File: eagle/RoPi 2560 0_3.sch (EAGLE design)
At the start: 49 parts, among them J1 AVR_SPI_PRG_6PTH, U1 ATMEGA2560AU, U2 MAX3378EEUD, U3 L298_BRIDGE_DRIVER, U4 L298_BRIDGE_DRIVER, Y1 16M

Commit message: Leaving 2nd revision board as-is; will not be ordering 0.2 board.
0.3 is a complete re-routing and layout adjustment. The ATmega has been
moved closer to the bottom left corner. The slot for the camera cable has
been adjusted to the left a bit to better sit squarely over the connector.

The reset switch and passives have been moved over the ethernet connector
adjacent to the FTDI header. The ISP header has also been moved away from
the edge to allow a normal IDC connector to fit.

Pullups have been added to the 5V side of the I2C bus.

The motor controller region has been spread out slightly for easier soldering.

Still need to finish routing the level shifter for the Pi's I2C and UART,
all of the ATmega's UARTS, ISP, motor control signals, and power.
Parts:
- removed AREF: (no value), pinhead:PINHD-1X1
- added C11: 100n, SparkFun-Passives:CAP0603-CAP
- added R4, R5: 10K, SparkFun-Passives:RESISTOR0603-RES
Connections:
- net 5V: now also C11.1, R4.2, R5.2
- net AREF: no longer AREF.1
- net AVR_SCL: now also R5.1
- net AVR_SDA: now also R4.1
- net GND: now also C11.2
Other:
- moved on the sheet: C4
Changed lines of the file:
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@@
 <part name="GND3" library="SparkFun-Aesthetics" deviceset="GND" device=""/>
 <part name="C3" library="SparkFun-Passives" deviceset="CAP" device="0603-CAP" value="100n"/>
-<part name="C4" library="SparkFun-Passives" deviceset="CAP" device="0603-CAP" value="100n"/>
+<part name="C11" library="SparkFun-Passives" deviceset="CAP" device="0603-CAP" value="100n"/>
 <part name="SUPPLY4" library="SparkFun-Aesthetics" deviceset="5V" device=""/>
 <part name="SUPPLY5" library="SparkFun-Aesthetics" deviceset="3.3V" device=""/>
@@
 <part name="L1" library="dab5267" deviceset="L-US" device="" value="10uH"/>
 <part name="C15" library="SparkFun-Passives" deviceset="CAP" device="0603-CAP" value="100n"/>
-<part name="AREF" library="pinhead" deviceset="PINHD-1X1" device=""/>
 <part name="SUPPLY1" library="SparkFun-Aesthetics" deviceset="5V" device=""/>
 <part name="SUPPLY2" library="SparkFun-Aesthetics" deviceset="5V" device=""/>
@@
 <part name="SUPPLY14" library="SparkFun-Aesthetics" deviceset="5V" device=""/>
 <part name="S1" library="SparkFun-Electromechanical" deviceset="SWITCH-MOMENTARY-2" device="SMD-4"/>
+<part name="C4" library="SparkFun-Passives" deviceset="CAP" device="0603-CAP" value="100n"/>
+<part name="R4" library="SparkFun-Passives" deviceset="RESISTOR" device="0603-RES" value="10K"/>
+<part name="R5" library="SparkFun-Passives" deviceset="RESISTOR" device="0603-RES" value="10K"/>
 </parts>
 <sheets>
@@
 <instance part="GND3" gate="1" x="134.62" y="99.06"/>
 <instance part="C3" gate="G$1" x="-30.48" y="111.76" rot="R90"/>
-<instance part="C4" gate="G$1" x="-12.7" y="86.36"/>
+<instance part="C11" gate="G$1" x="-12.7" y="86.36"/>
 <instance part="SUPPLY4" gate="G$1" x="63.5" y="279.4"/>
 <instance part="SUPPLY5" gate="G$1" x="5.08" y="297.18"/>
@@
 <attribute name="VALUE" x="-13.716" y="101.981" size="1.778" layer="96"/>
 </instance>
-<instance part="AREF" gate="G$1" x="-20.32" y="134.62"/>
 <instance part="SUPPLY1" gate="G$1" x="50.8" y="182.88"/>
 <instance part="SUPPLY2" gate="G$1" x="134.62" y="116.84"/>
 <instance part="SUPPLY3" gate="G$1" x="-5.08" y="142.24"/>
-<instance part="SUPPLY7" gate="G$1" x="134.62" y="35.56"/>
+<instance part="SUPPLY7" gate="G$1" x="134.62" y="43.18"/>
 <instance part="SUPPLY14" gate="G$1" x="137.16" y="83.82"/>
 <instance part="S1" gate="G$1" x="-66.04" y="127" smashed="yes">
 <attribute name="NAME" x="-68.58" y="129.54" size="1.778" layer="95"/>
 </instance>
+<instance part="C4" gate="G$1" x="154.94" y="35.56"/>
+<instance part="R4" gate="G$1" x="55.88" y="175.26" rot="R90"/>
+<instance part="R5" gate="G$1" x="63.5" y="175.26" rot="R90"/>
 </instances>
 <busses>
@@
 <segment>
 <pinref part="U2" gate="G$1" pin="IO_VCC2"/>
-<wire x1="48.26" y1="165.1" x2="81.28" y2="165.1" width="0.1524" layer="91"/>
+<wire x1="48.26" y1="165.1" x2="63.5" y2="165.1" width="0.1524" layer="91"/>
 <label x="68.58" y="165.1" size="1.778" layer="95"/>
+<pinref part="R5" gate="G$1" pin="1"/>
+<wire x1="63.5" y1="165.1" x2="81.28" y2="165.1" width="0.1524" layer="91"/>
+<wire x1="63.5" y1="170.18" x2="63.5" y2="165.1" width="0.1524" layer="91"/>
+<junction x="63.5" y="165.1"/>
 </segment>
 </net>
@@
 <segment>
 <pinref part="U2" gate="G$1" pin="IO_VCC1"/>
-<wire x1="48.26" y1="167.64" x2="81.28" y2="167.64" width="0.1524" layer="91"/>
+<wire x1="48.26" y1="167.64" x2="55.88" y2="167.64" width="0.1524" layer="91"/>
 <label x="68.58" y="167.64" size="1.778" layer="95"/>
+<pinref part="R4" gate="G$1" pin="1"/>
+<wire x1="55.88" y1="167.64" x2="81.28" y2="167.64" width="0.1524" layer="91"/>
+<wire x1="55.88" y1="170.18" x2="55.88" y2="167.64" width="0.1524" layer="91"/>
+<junction x="55.88" y="167.64"/>
 </segment>
 </net>
@@
 <wire x1="134.62" y1="27.94" x2="134.62" y2="30.48" width="0.1524" layer="91"/>
 <wire x1="134.62" y1="30.48" x2="134.62" y2="33.02" width="0.1524" layer="91"/>
-<wire x1="134.62" y1="33.02" x2="134.62" y2="35.56" width="0.1524" layer="91"/>
+<wire x1="134.62" y1="33.02" x2="134.62" y2="40.64" width="0.1524" layer="91"/>
+<wire x1="134.62" y1="40.64" x2="134.62" y2="43.18" width="0.1524" layer="91"/>
 <wire x1="137.16" y1="25.4" x2="134.62" y2="25.4" width="0.1524" layer="91"/>
 <pinref part="U$2" gate="G$1" pin="5"/>
@@
 <junction x="134.62" y="33.02"/>
 <pinref part="SUPPLY7" gate="G$1" pin="5V"/>
+<pinref part="C4" gate="G$1" pin="1"/>
+<wire x1="154.94" y1="40.64" x2="134.62" y2="40.64" width="0.1524" layer="91"/>
+<junction x="134.62" y="40.64"/>
 </segment>
 <segment>
@@
 <junction x="-5.08" y="96.52"/>
 <junction x="-5.08" y="93.98"/>
-<pinref part="C4" gate="G$1" pin="1"/>
+<pinref part="C11" gate="G$1" pin="1"/>
 <wire x1="-5.08" y1="91.44" x2="-12.7" y2="91.44" width="0.1524" layer="91"/>
 <pinref part="C12" gate="G$1" pin="1"/>
@@
 <wire x1="50.8" y1="180.34" x2="50.8" y2="182.88" width="0.1524" layer="91"/>
 <pinref part="SUPPLY1" gate="G$1" pin="5V"/>
+<pinref part="R4" gate="G$1" pin="2"/>
+<wire x1="50.8" y1="180.34" x2="55.88" y2="180.34" width="0.1524" layer="91"/>
+<pinref part="R5" gate="G$1" pin="2"/>
+<wire x1="55.88" y1="180.34" x2="63.5" y2="180.34" width="0.1524" layer="91"/>
+<junction x="55.88" y="180.34"/>
+<junction x="50.8" y="180.34"/>
 </segment>
 </net>
@@
 <pinref part="C12" gate="G$1" pin="2"/>
 <wire x1="-22.86" y1="83.82" x2="-22.86" y2="81.28" width="0.1524" layer="91"/>
-<pinref part="C4" gate="G$1" pin="2"/>
+<pinref part="C11" gate="G$1" pin="2"/>
 <wire x1="-12.7" y1="83.82" x2="-12.7" y2="81.28" width="0.1524" layer="91"/>
 <junction x="-33.02" y="81.28"/>
@@
 <junction x="154.94" y="25.4"/>
 <junction x="154.94" y="30.48"/>
+<pinref part="C4" gate="G$1" pin="2"/>
+<junction x="154.94" y="33.02"/>
 </segment>
 <segment>
@@
 <pinref part="C3" gate="G$1" pin="2"/>
 <pinref part="U1" gate="1" pin="AREF"/>
-<wire x1="-27.94" y1="111.76" x2="-25.4" y2="111.76" width="0.1524" layer="91"/>
-<pinref part="AREF" gate="G$1" pin="1"/>
-<wire x1="-25.4" y1="111.76" x2="-2.54" y2="111.76" width="0.1524" layer="91"/>
-<wire x1="-22.86" y1="134.62" x2="-25.4" y2="134.62" width="0.1524" layer="91"/>
-<wire x1="-25.4" y1="134.62" x2="-25.4" y2="111.76" width="0.1524" layer="91"/>
-<junction x="-25.4" y="111.76"/>
-</segment>
-</net>
+<wire x1="-27.94" y1="111.76" x2="-2.54" y2="111.76" width="0.1524" layer="91"/>
+</segment>
+</net>

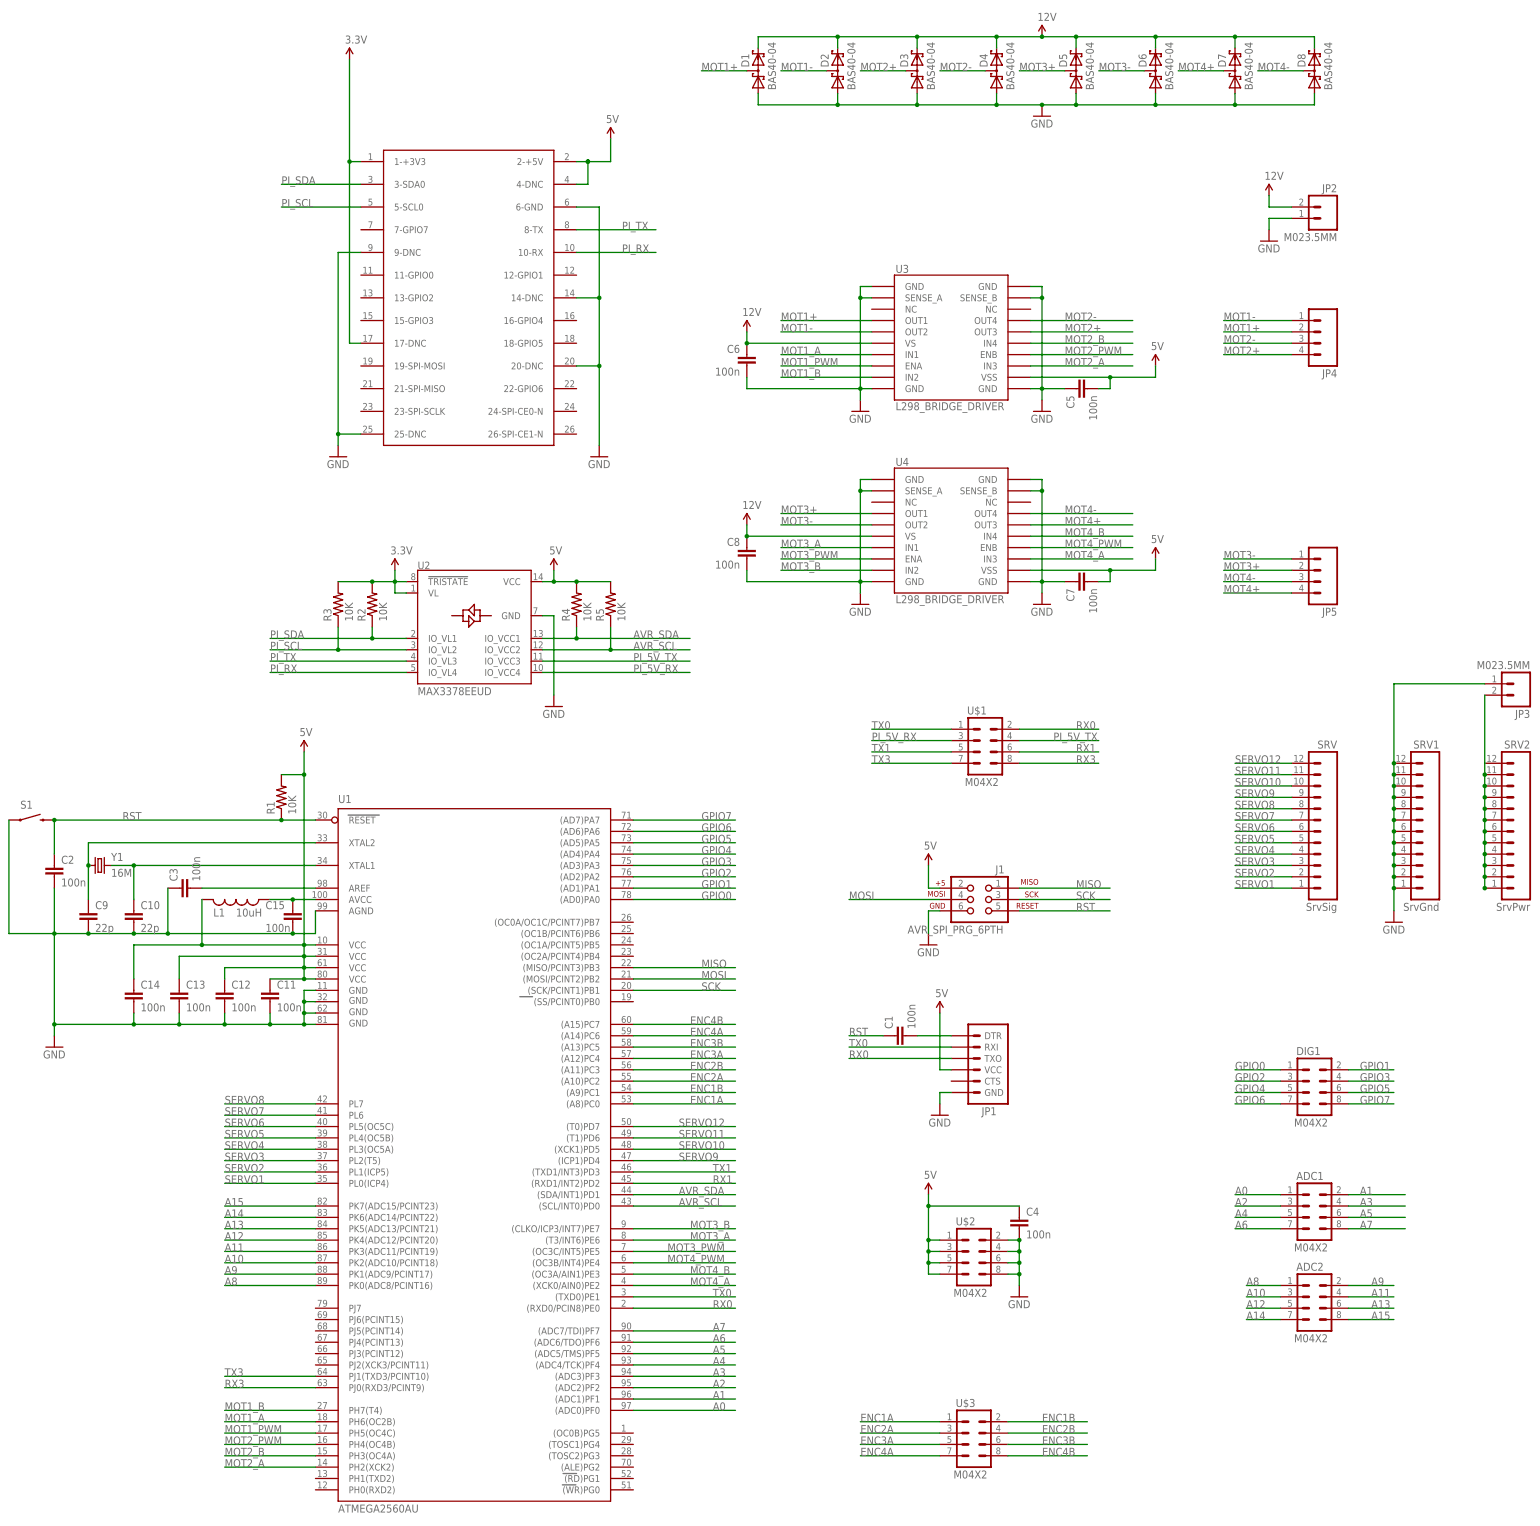
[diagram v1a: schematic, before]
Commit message: Updated name to RoverPi, moved arduino library into /arduino/RoverPi
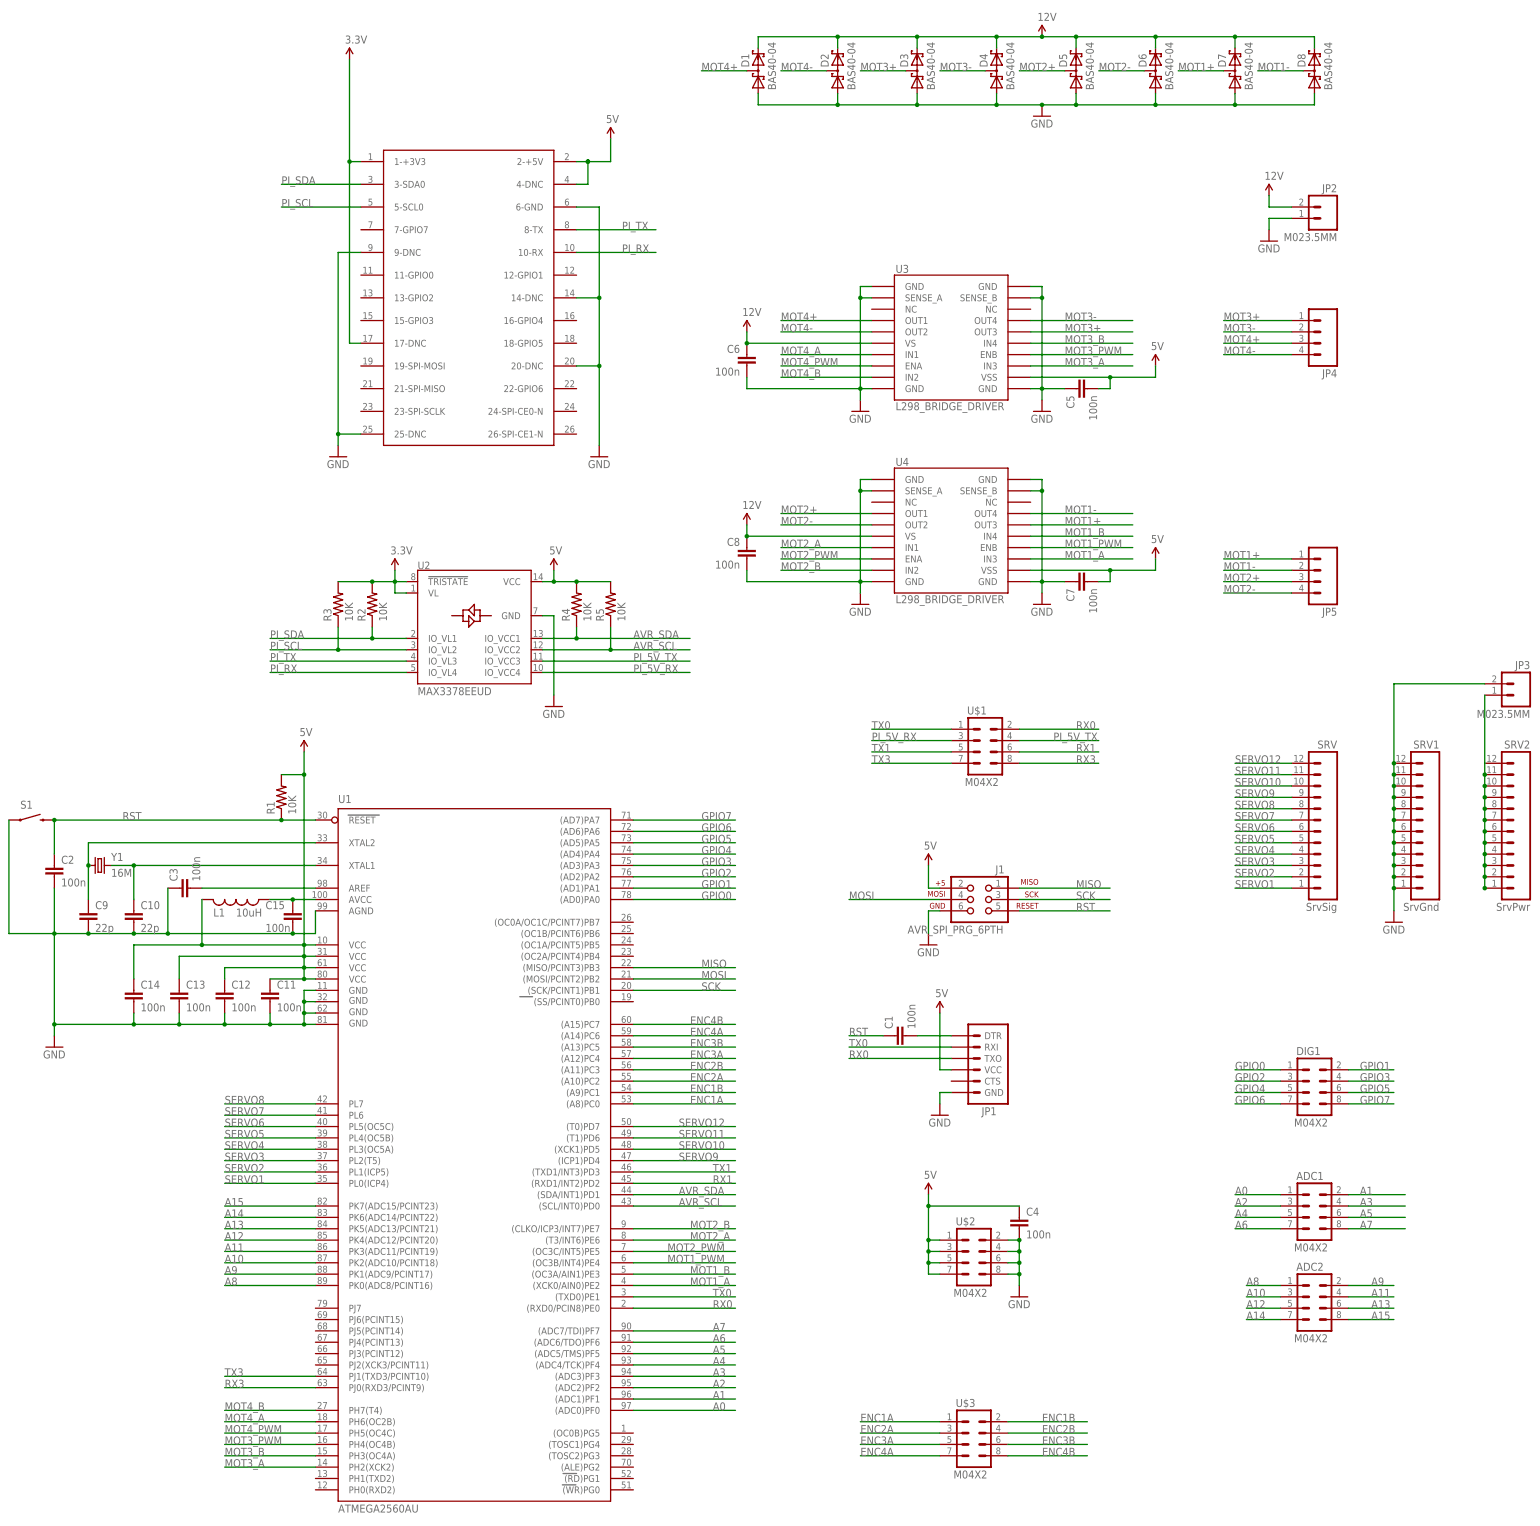
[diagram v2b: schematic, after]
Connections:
- net GND: now also JP3.2; no longer JP3.1
- net MOT1+: now also D7.C1A2, JP5.1, U4.OUT3; no longer D1.C1A2, JP4.2, U3.OUT1
- net MOT1-: now also D8.C1A2, JP5.2, U4.OUT4; no longer D2.C1A2, JP4.1, U3.OUT2
- net MOT1_A: now also U1.(XCK0/AIN0)PE2, U4.IN3; no longer U1.PH6(OC2B), U3.IN1
- net MOT1_B: now also U1.(OC3A/AIN1)PE3, U4.IN4; no longer U1.PH7(T4), U3.IN2
- net MOT1_PWM: now also U1.(OC3B/INT4)PE4, U4.ENB; no longer U1.PH5(OC4C), U3.ENA
- net MOT2+: now also D5.C1A2, JP5.3, U4.OUT1; no longer D3.C1A2, JP4.4, U3.OUT3
- net MOT2-: now also D6.C1A2, JP5.4, U4.OUT2; no longer D4.C1A2, JP4.3, U3.OUT4
- net MOT2_A: now also U1.(T3/INT6)PE6, U4.IN1; no longer U1.PH2(XCK2), U3.IN3
- net MOT2_B: now also U1.(CLKO/ICP3/INT7)PE7, U4.IN2; no longer U1.PH3(OC4A), U3.IN4
- net MOT2_PWM: now also U1.(OC3C/INT5)PE5, U4.ENA; no longer U1.PH4(OC4B), U3.ENB
- net MOT3+: now also D3.C1A2, JP4.1, U3.OUT3; no longer D5.C1A2, JP5.2, U4.OUT1
- net MOT3-: now also D4.C1A2, JP4.2, U3.OUT4; no longer D6.C1A2, JP5.1, U4.OUT2
- net MOT3_A: now also U1.PH2(XCK2), U3.IN3; no longer U1.(T3/INT6)PE6, U4.IN1
- net MOT3_B: now also U1.PH3(OC4A), U3.IN4; no longer U1.(CLKO/ICP3/INT7)PE7, U4.IN2
- net MOT3_PWM: now also U1.PH4(OC4B), U3.ENB; no longer U1.(OC3C/INT5)PE5, U4.ENA
- net MOT4+: now also D1.C1A2, JP4.3, U3.OUT1; no longer D7.C1A2, JP5.4, U4.OUT3
- net MOT4-: now also D2.C1A2, JP4.4, U3.OUT2; no longer D8.C1A2, JP5.3, U4.OUT4
- net MOT4_A: now also U1.PH6(OC2B), U3.IN1; no longer U1.(XCK0/AIN0)PE2, U4.IN3
- net MOT4_B: now also U1.PH7(T4), U3.IN2; no longer U1.(OC3A/AIN1)PE3, U4.IN4
- net MOT4_PWM: now also U1.PH5(OC4C), U3.ENA; no longer U1.(OC3B/INT4)PE4, U4.ENB
- net N$1: now also JP3.1; no longer JP3.2
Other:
- moved on the sheet: JP3
